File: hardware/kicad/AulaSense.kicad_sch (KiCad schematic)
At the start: 0 parts

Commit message: feat(hw): simbolos ESP32 DevKit V1 con pinout y tipos electricos
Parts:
- added J1: ESP32_DevKitV1_Header_Left, symbol AulaSense:ESP32_DevKitV1_Header_Left
- added J2: ESP32_DevKitV1_Header_Right, symbol AulaSense:ESP32_DevKitV1_Header_Right
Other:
- company: (none) -> AulaSense S.A.S
- title: (none) -> AulaSense - Monitor ambiental
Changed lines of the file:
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@@
 	(generator_version "10.0")
 	(paper "A4")
+	(title_block
+		(title "AulaSense - Monitor ambiental")
+		(date "2026-08-10")
+		(rev "0.1")
+		(company "AulaSense S.A.S")
+		(comment 1 "Juan Sebastián Sierra Arenas")
+		(comment 2 "Ficha 2879896 — Desarrollo de Productos Electrónicos")
+		(comment 3 "SENA CEET")
+	)
+	(symbol
+		(lib_id "AulaSense:ESP32_DevKitV1_Header_Right")
+		(at 165.1 77.47 0)
+		(mirror y)
+		(unit 1)
+		(body_style 1)
+		(exclude_from_sim no)
+		(in_bom yes)
+		(on_board yes)
+		(in_pos_files yes)
+		(dnp no)
+		(property "Reference" "J2"
+			(at 162.56 76.1999 0)
+			(show_name no)
+			(do_not_autoplace no)
+			(effects
+				(font
+					(size 1.27 1.27)
+				)
+				(justify left)
+			)
+		)
+		(property "Value" "ESP32_DevKitV1_Header_Right"
+			(at 165.1 97.79 0)
+			(show_name no)
+			(do_not_autoplace no)
+			(effects
+				(font
+					(size 1.27 1.27)
+				)
+			)
+		)
+		(property "Footprint" ""
+			(at 165.1 77.47 0)
+			(hide yes)
+			(show_name no)
+			(do_not_autoplace no)
+			(effects
+				(font
+					(size 1.27 1.27)
+				)
+			)
+		)
+		(property "Datasheet" ""
+			(at 165.1 77.47 0)
+			(hide yes)
+			(show_name no)
+			(do_not_autoplace no)
+			(effects
+				(font
+					(size 1.27 1.27)
+				)
+			)
+		)
+		(property "Description" "Generic connector, single row, 01x15, script generated (kicad-library-utils/schlib/autogen/connector/)"
+			(at 165.1 77.47 0)
+			(hide yes)
+			(show_name no)
+			(do_not_autoplace no)
+			(effects
+				(font
+					(size 1.27 1.27)
+				)
+			)
+		)
+		(pin "9"
+		)
+		(pin "4"
+		)
+		(pin "2"
+		)
+		(pin "5"
+		)
+		(pin "12"
+		)
+		(pin "6"
+		)
+		(pin "11"
+		)
+		(pin "15"
+		)
+		(pin "3"
+		)
+		(pin "8"
+		)
+		(pin "13"
+		)
+		(pin "1"
+		)
+		(pin "7"
+		)
+		(pin "10"
+		)
+		(pin "14"
+		)
+		(instances
+			(project "AulaSense"
+				(path "/845ab8da-6aae-42ab-960f-99c5342b87b9"
+					(reference "J2")
+					(unit 1)
+				)
+			)
+		)
+	)
+	(symbol
+		(lib_id "AulaSense:ESP32_DevKitV1_Header_Left")
+		(at 123.19 78.74 0)
+		(unit 1)
+		(body_style 1)
+		(exclude_from_sim no)
+		(in_bom yes)
+		(on_board yes)
+		(in_pos_files yes)
+		(dnp no)
+		(fields_autoplaced yes)
+		(property "Reference" "J1"
+			(at 125.73 77.4699 0)
+			(show_name no)
+			(do_not_autoplace no)
+			(effects
+				(font
+					(size 1.27 1.27)
+				)
+				(justify left)
+			)
+		)
+		(property "Value" "ESP32_DevKitV1_Header_Left"
+			(at 125.73 80.0099 0)
+			(show_name no)
+			(do_not_autoplace no)
+			(effects
+				(font
+					(size 1.27 1.27)
+				)
+				(justify left)
+			)
+		)
+		(property "Footprint" ""
+			(at 123.19 78.74 0)
+			(hide yes)
+			(show_name no)
+			(do_not_autoplace no)
+			(effects
+				(font
+					(size 1.27 1.27)
+				)
+			)
+		)
+		(property "Datasheet" ""
+			(at 123.19 78.74 0)
+			(hide yes)
+			(show_name no)
+			(do_not_autoplace no)
+			(effects
+				(font
+					(size 1.27 1.27)
+				)
+			)
+		)
+		(property "Description" "Generic connector, single row, 01x15, script generated (kicad-library-utils/schlib/autogen/connector/)"
+			(at 123.19 78.74 0)
+			(hide yes)
+			(show_name no)
+			(do_not_autoplace no)
+			(effects
+				(font
+					(size 1.27 1.27)
+				)
+			)
+		)
+		(pin "13"
+		)
+		(pin "2"
+		)
+		(pin "5"
+		)
+		(pin "9"
+		)
+		(pin "15"
+		)
+		(pin "10"
+		)
+		(pin "14"
+		)
+		(pin "1"
+		)
+		(pin "11"
+		)
+		(pin "7"
+		)
+		(pin "8"
+		)
+		(pin "6"
+		)
+		(pin "4"
+		)
+		(pin "3"
+		)
+		(pin "12"
+		)
+		(instances
+			(project "AulaSense"
+				(path "/845ab8da-6aae-42ab-960f-99c5342b87b9"
+					(reference "J1")
+					(unit 1)
+				)
+			)
+		)
+	)
 	(sheet_instances
 		(path "/"

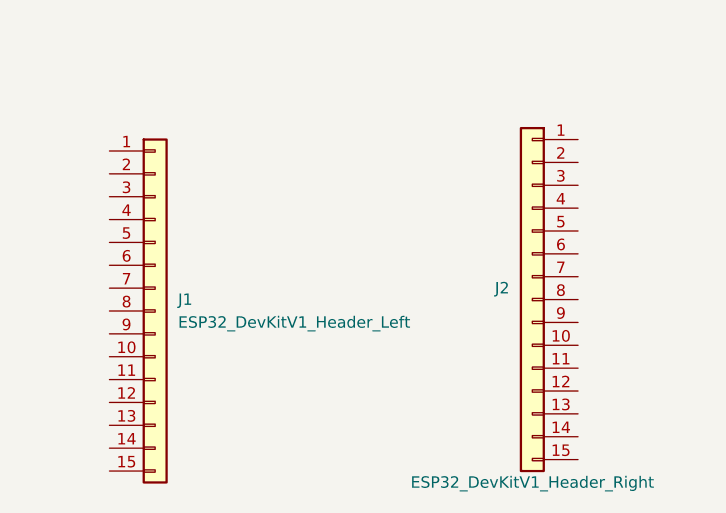
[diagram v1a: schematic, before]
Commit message: feat(hw): asignacion de GPIO y etiquetas de senal en headers ESP32
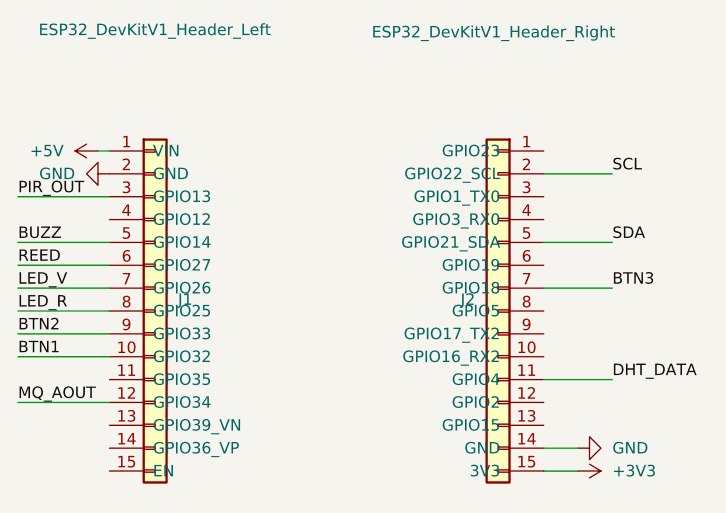
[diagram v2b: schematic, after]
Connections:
- net DHT_DATA: now reaches J2.11 (GPIO4)
- net GND: now reaches J2.14 (GND)
- net GND: now also J1.2 (GND)
- net +3V3: now reaches J2.15 (3V3)
- net SCL: now reaches J2.2 (GPIO22_SCL)
- net SDA: now reaches J2.5 (GPIO21_SDA)
- net BTN3: now reaches J2.7 (GPIO18)
- net +5V: now reaches J1.1 (VIN)
- net BTN1: now reaches J1.10 (GPIO32)
- net MQ_AOUT: now reaches J1.12 (GPIO34)
- net PIR_OUT: now reaches J1.3 (GPIO13)
- net BUZZ: now reaches J1.5 (GPIO14)
- net REED: now reaches J1.6 (GPIO27)
- net LED_V: now reaches J1.7 (GPIO26)
- net LED_R: now reaches J1.8 (GPIO25)
- net BTN2: now reaches J1.9 (GPIO33)

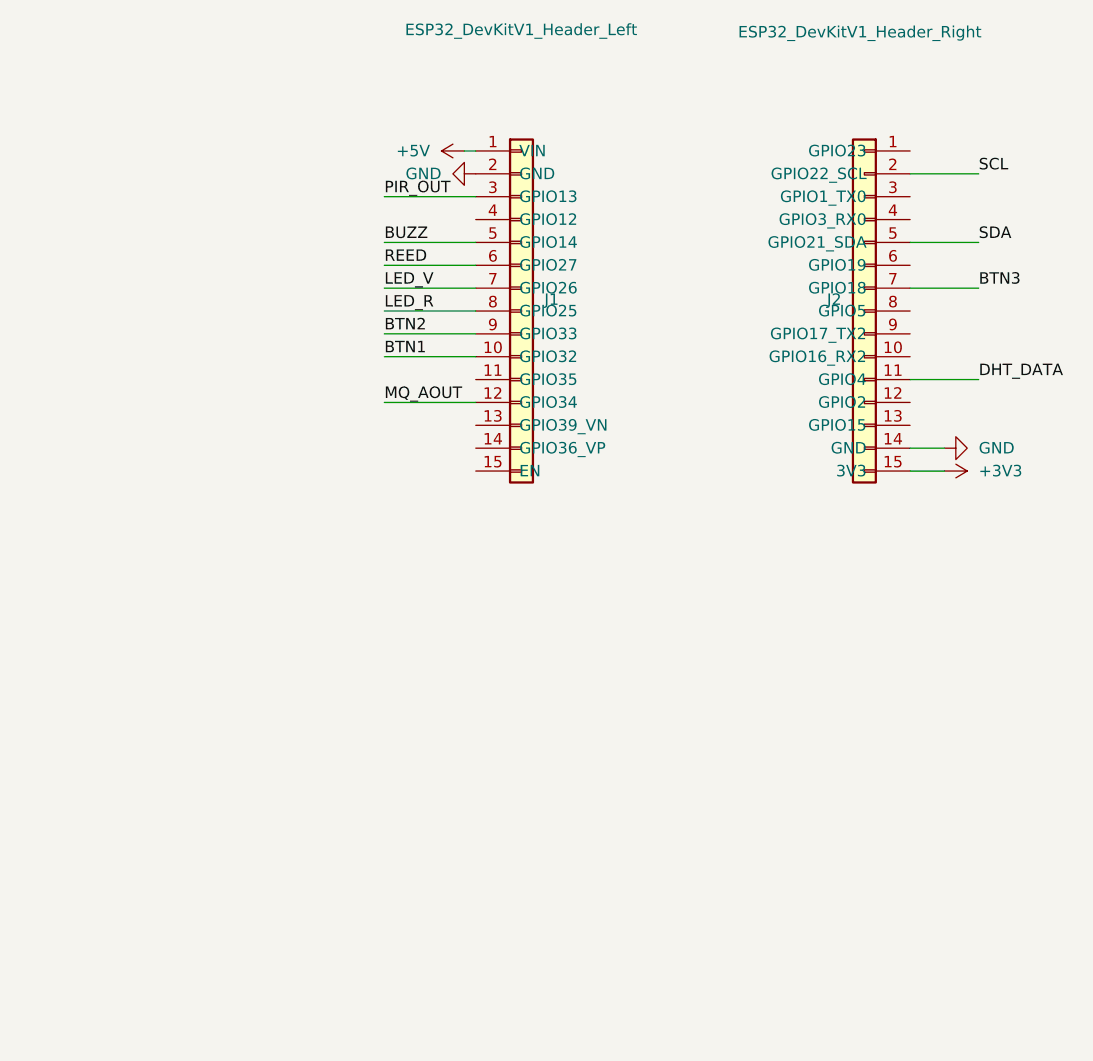
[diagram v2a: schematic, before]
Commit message: feat(hw): bloque de alimentacion con proteccion y PWR_FLAG
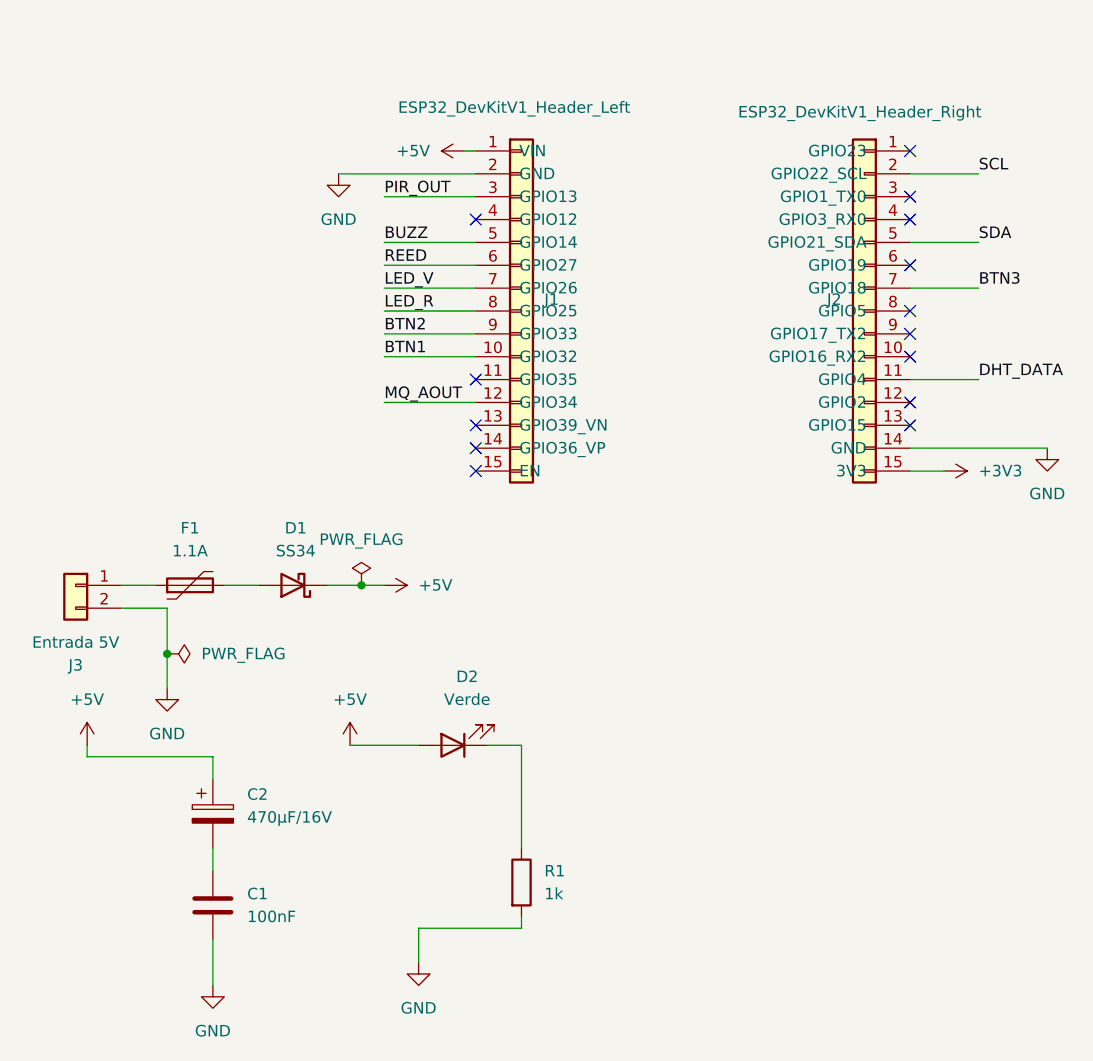
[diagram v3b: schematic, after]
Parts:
- added C1: 100nF, symbol Device:C
- added C2: 470µF/16V, symbol Device:C_Polarized
- added D1: SS34, symbol Device:D_Schottky
- added D2: Verde, symbol Device:LED
- added F1: 1.1A, symbol Device:Polyfuse
- added J3: Entrada 5V, symbol Connector_Generic:Conn_01x02
- added R1: 1k, symbol Device:R
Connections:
- net +5V: now also C2.1, D1.1 (K), D2.2 (A)
- net GND: now also C1.2, J3.2 (Pin_2), R1.2
- new net: C1.1, C2.2
- new net: D2.1 (K), R1.1
- new net: F1.1, J3.1 (Pin_1)
- new net: D1.2 (A), F1.2
- no-connect marks 0 -> 14

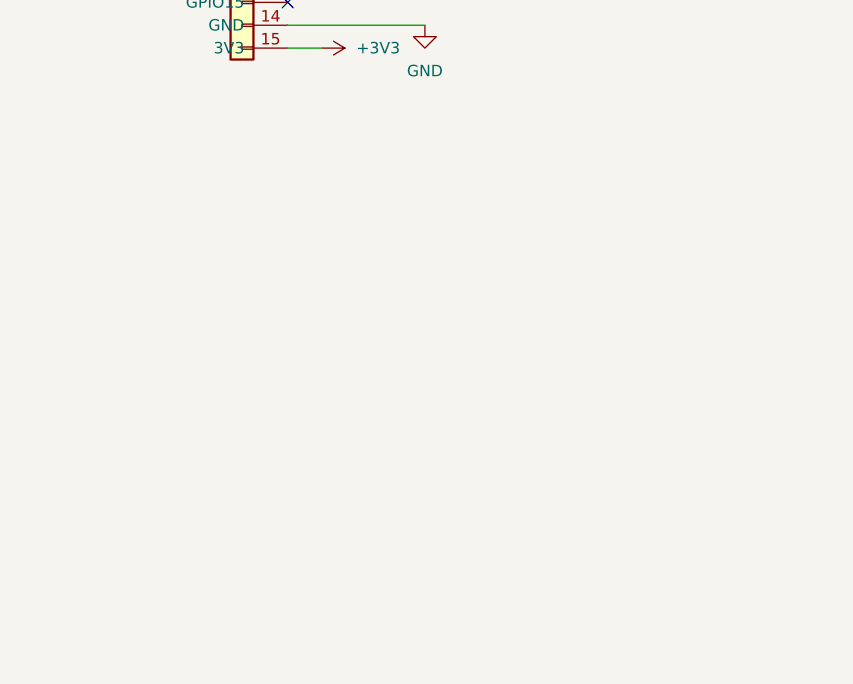
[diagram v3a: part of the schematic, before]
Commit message: feat(hw): bloque de botones con antirrebote RC
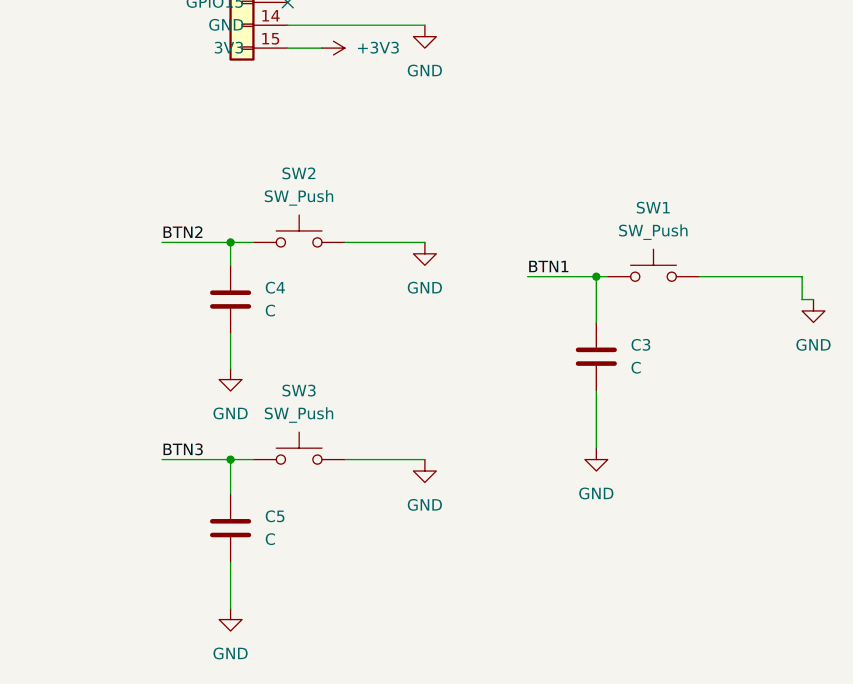
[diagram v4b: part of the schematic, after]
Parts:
- added C3, C4, C5: C, symbol Device:C
- added SW1, SW2, SW3: SW_Push, symbol Switch:SW_Push
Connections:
- net BTN1: now also C3.1, SW1.1
- net BTN2: now also C4.1, SW2.1
- net BTN3: now also C5.1, SW3.1
- net GND: now also C3.2, C4.2, C5.2, SW1.2, SW2.2, SW3.2

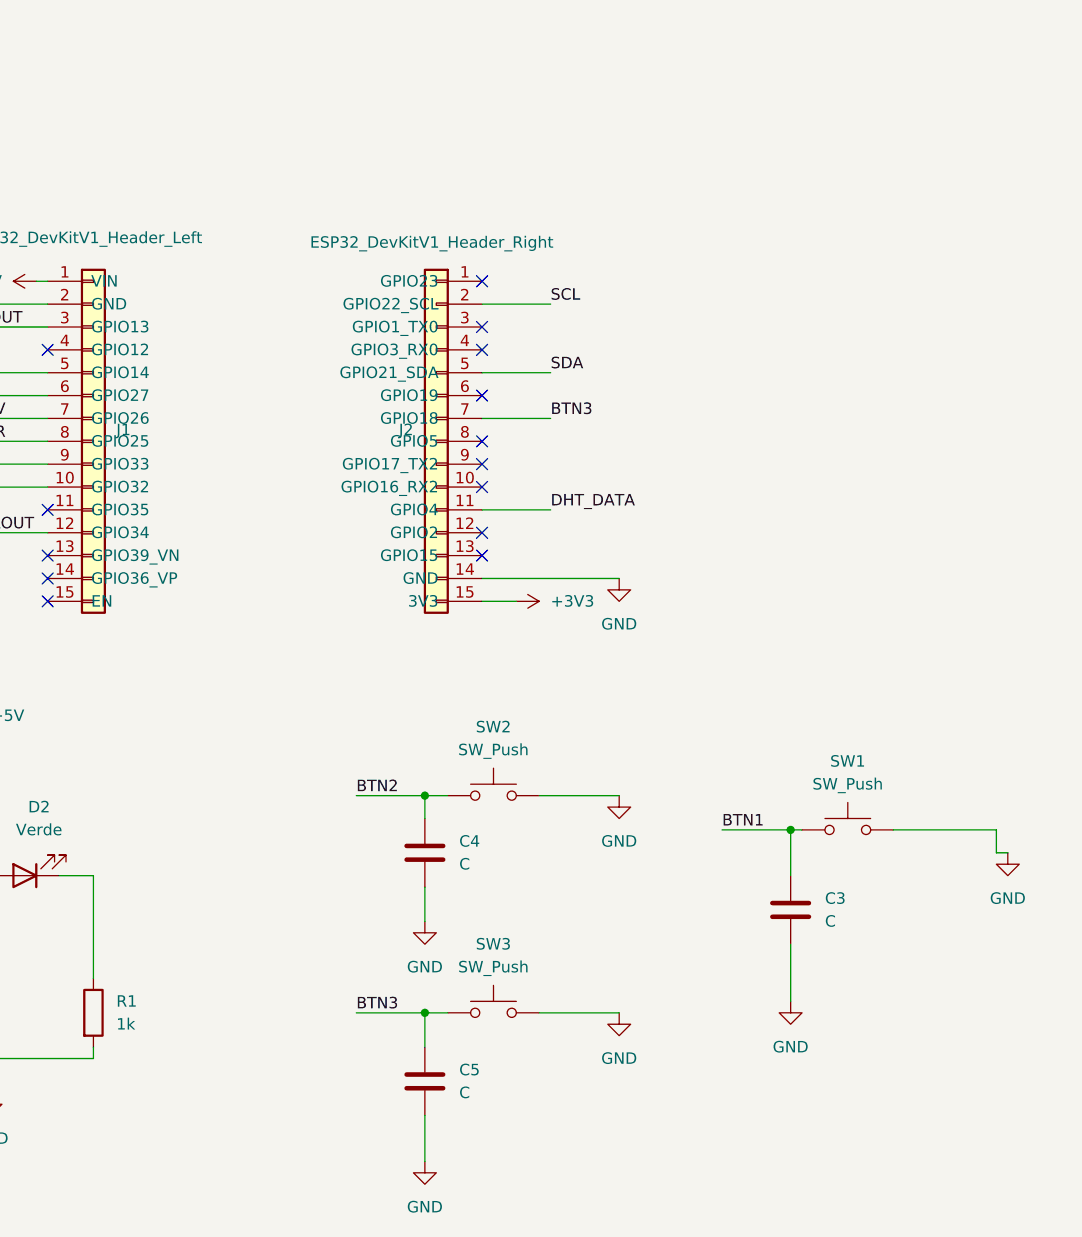
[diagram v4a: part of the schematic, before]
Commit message: feat(hw): bloque de notificacion con LEDs y buzzer
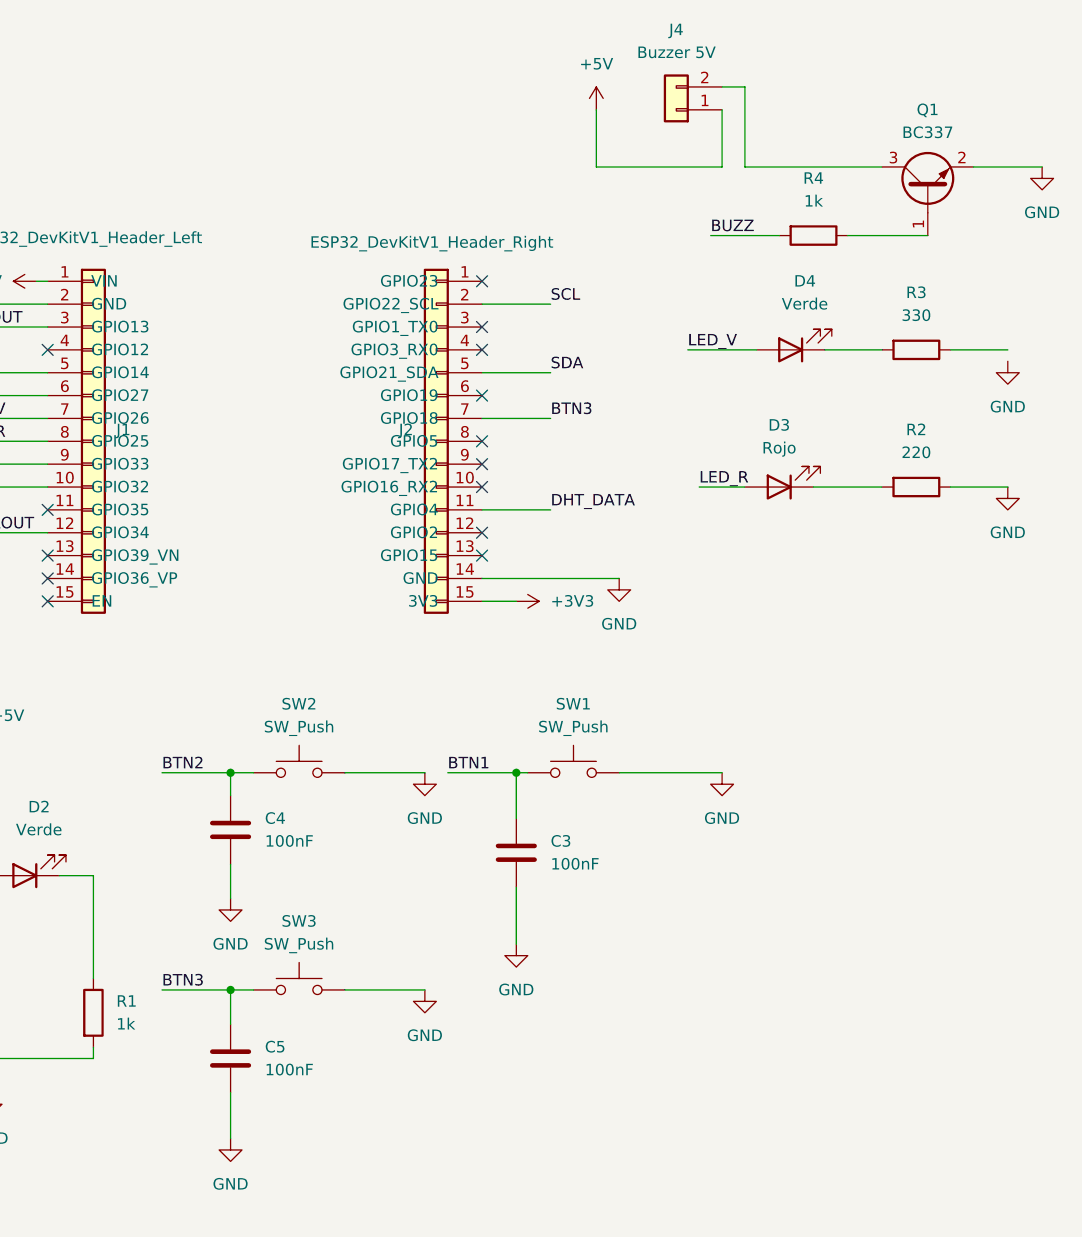
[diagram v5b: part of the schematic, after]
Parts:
- added D3: Rojo, symbol Device:LED
- added D4: Verde, symbol Device:LED
- added J4: Buzzer 5V, symbol Connector_Generic:Conn_01x02
- added Q1: BC337, symbol Transistor_BJT:Q_NPN_BEC
- added R2: 220, symbol Device:R
- added R3: 330, symbol Device:R
- added R4: 1k, symbol Device:R
- C3, C4, C5: value C -> 100nF
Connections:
- net +5V: now also J4.1 (Pin_1)
- net BUZZ: now also R4.2
- net GND: now also Q1.2 (E), R2.1
- net LED_R: now also D3.2 (A)
- net LED_V: now also D4.2 (A)
- new net: D4.1 (K), R3.2
- new net: D3.1 (K), R2.2
- new net: J4.2 (Pin_2), Q1.3 (C)
- new net: Q1.1 (B), R4.1
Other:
- moved on the sheet: C3, C4, C5, SW1, SW2, SW3
